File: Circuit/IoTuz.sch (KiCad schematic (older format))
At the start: 29 parts, among them P1 Alligator Connector, P2 BATTERY, P3 USB_5PIN_SHELL, P4 LED_1, P5 LED_2, P6 CONN_01X20, P7 CONN_01X20, Q1 S8050, Q2 S8050, Q3 FDN340P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

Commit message: Updated Alligator tabs
Incomplete.  Included to provide ideas.
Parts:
- P1: footprint libs:aligator_pads -> libs:alligator_pads
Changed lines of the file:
@@
 F 0 "P1" H 6300 7700 50  0000 C CNN
 F 1 "Alligator Connector" V 6400 6950 50  0000 C CNN
-F 2 "libs:aligator_pads" H 6300 6950 50  0001 C CNN
+F 2 "libs:alligator_pads" H 6300 6950 50  0001 C CNN
 F 3 "" H 6300 6950 50  0000 C CNN
 	1    6300 6950

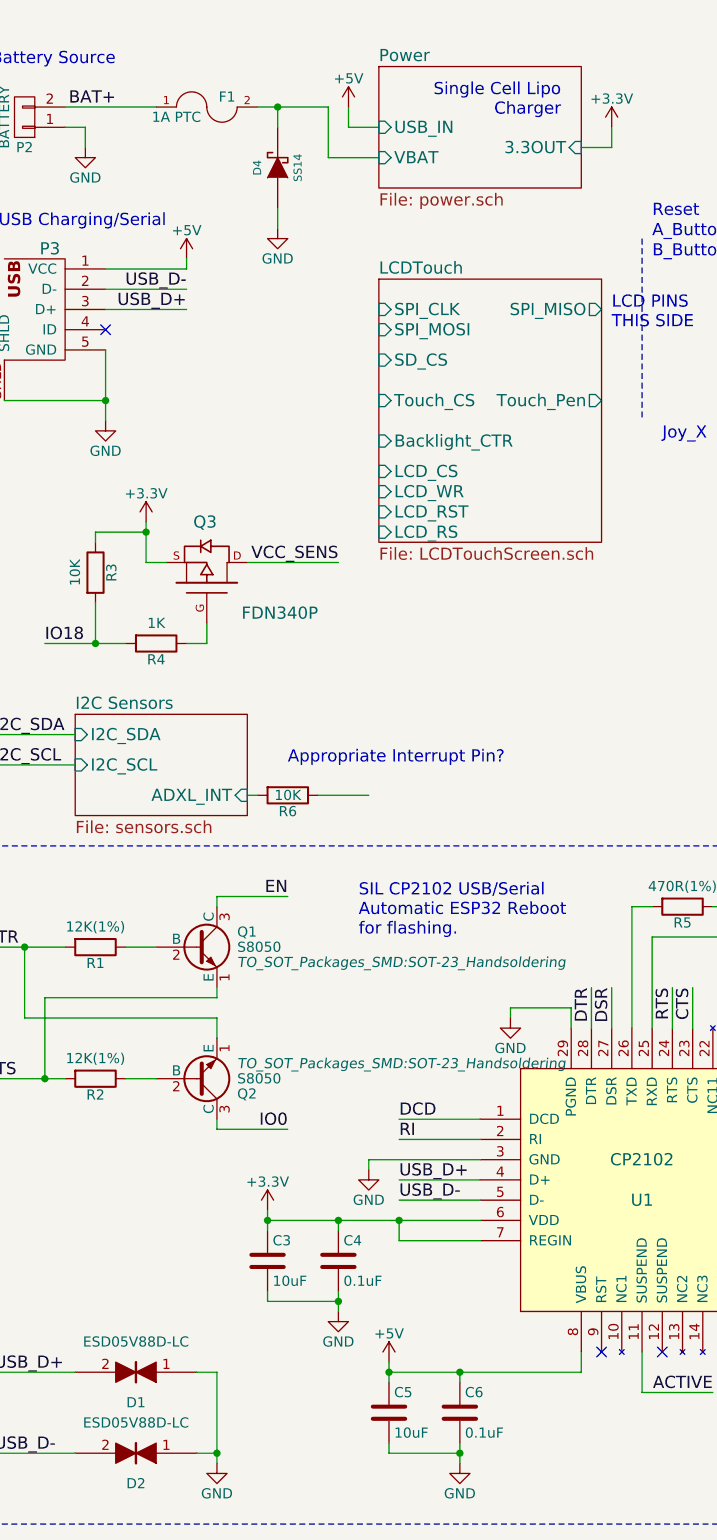
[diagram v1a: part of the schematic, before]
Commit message: BOM information to schematic. Power & main sheets mostly.
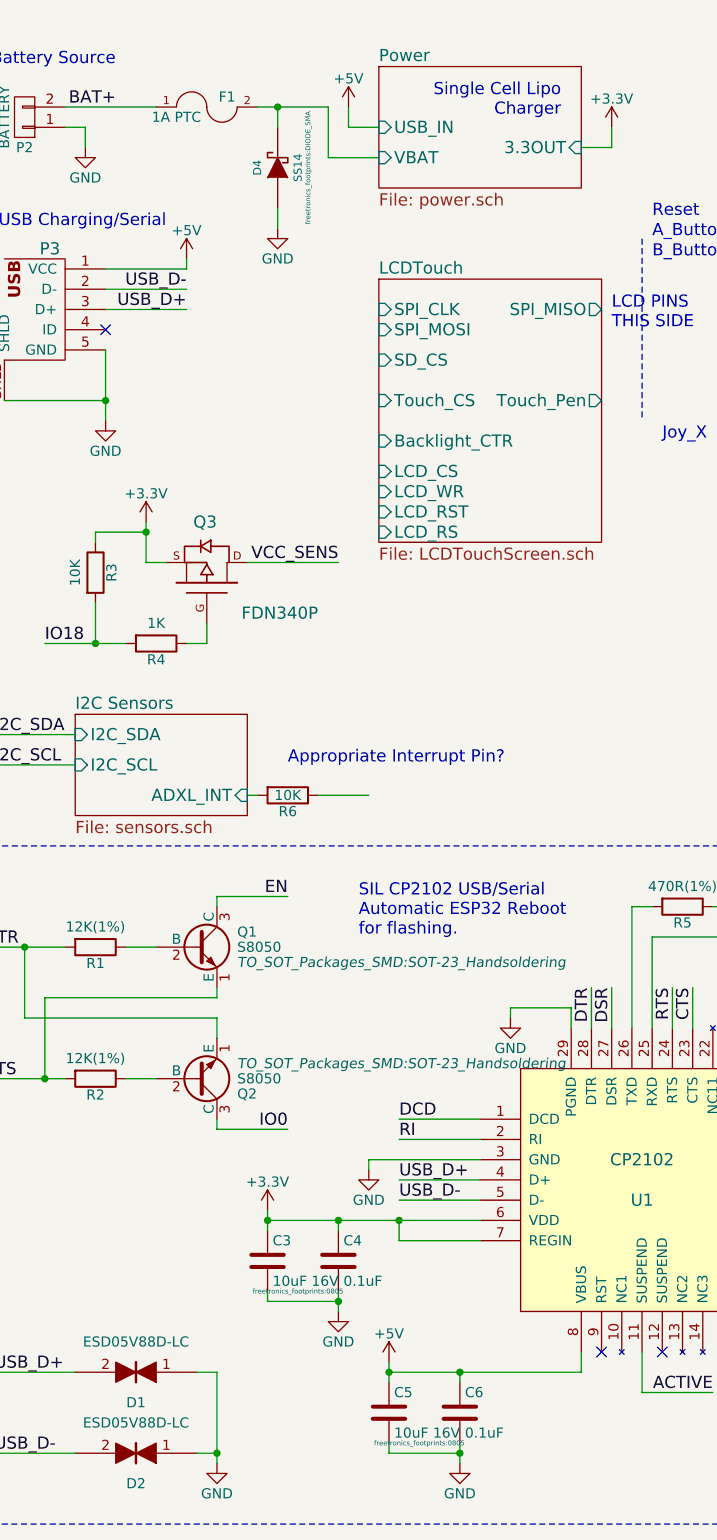
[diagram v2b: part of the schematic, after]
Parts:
- C3, C5: value 10uF -> 10uF 16V; footprint Capacitors_SMD:C_0603_HandSoldering -> freetronics_footprints:0805; Digikey PN (none) -> 1276-2399-1-ND; Link (none) -> http://www.digikey.com.au/product-detail/en/samsung-electro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; Manufacturer PN (none) -> CL21A106KOCLRNC; Unit Cost (none) -> 0.18
- C4, C6: Digikey PN (none) -> 311-1088-1-ND; Link (none) -> http://www.digikey.com.au/product-detail/en/yageo/CC0603KRX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; Manufacturer PN (none) -> CC0603KRX7R7BB104; Unit Cost (none) -> 0.10
- D4: Digikey PN (none) -> SS14CT-ND; Link (none) -> http://www.digikey.com.au/product-detail/en/fairchild-semic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; Manufacturer PN (none) -> SS14; Unit Cost (none) -> 0.39
- P1: footprint libs:alligator_pads -> libs:aligator_pads
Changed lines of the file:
@@
 BAT+
-$Comp
-L DIODE_SCHOTTKY D4
-U 1 1 57FB66B6
-P 2000 1150
-F 0 "D4" H 2000 1250 40  0000 C CNN
-F 1 "SS14" H 2000 1050 40  0000 C CNN
-F 2 "freetronics_footprints:DIODE_SMA" H 2000 1150 60  0001 C CNN
-F 3 "" H 2000 1150 60  0000 C CNN
-	1    2000 1150
-	0    -1   -1   0
-$EndComp
 $Comp
 L GND #PWR03
@@
 $EndComp
 $Comp
-L C C3
-U 1 1 580787A7
-P 1950 6550
-F 0 "C3" H 1975 6650 50  0000 L CNN
-F 1 "10uF" H 1975 6450 50  0000 L CNN
-F 2 "Capacitors_SMD:C_0603_HandSoldering" H 1988 6400 50  0001 C CNN
-F 3 "" H 1950 6550 50  0000 C CNN
-	1    1950 6550
-	1    0    0    -1
-$EndComp
-$Comp
 L C C4
 U 1 1 58078ABF
@@
 F 2 "Capacitors_SMD:C_0603_HandSoldering" H 2338 6400 50  0001 C CNN
 F 3 "" H 2300 6550 50  0000 C CNN
+F 4 "311-1088-1-ND" H 2300 6550 60  0001 C CNN "Digikey PN"
+F 5 "http://www.digikey.com.au/product-detail/en/yageo/CC0603KRX7R7BB104/311-1088-1-ND/302998" H 2300 6550 60  0001 C CNN "Link"
+F 6 "CC0603KRX7R7BB104" H 2300 6550 60  0001 C CNN "Manufacturer PN"
+F 7 "0.10" H 2300 6550 60  0001 C CNN "Unit Cost"
 	1    2300 6550
 	1    0    0    -1
@@
 F 3 "" H 2550 7050 50  0000 C CNN
 	1    2550 7050
-	1    0    0    -1
-$EndComp
-$Comp
-L C C5
-U 1 1 5807AA65
-P 2550 7300
-F 0 "C5" H 2575 7400 50  0000 L CNN
-F 1 "10uF" H 2575 7200 50  0000 L CNN
-F 2 "Capacitors_SMD:C_0603_HandSoldering" H 2588 7150 50  0001 C CNN
-F 3 "" H 2550 7300 50  0000 C CNN
-	1    2550 7300
-	1    0    0    -1
-$EndComp
-$Comp
-L C C6
-U 1 1 5807AADF
-P 2900 7300
-F 0 "C6" H 2925 7400 50  0000 L CNN
-F 1 "0.1uF" H 2925 7200 50  0000 L CNN
-F 2 "Capacitors_SMD:C_0603_HandSoldering" H 2938 7150 50  0001 C CNN
-F 3 "" H 2900 7300 50  0000 C CNN
-	1    2900 7300
 	1    0    0    -1
 $EndComp
@@
 F 0 "P1" H 6300 7700 50  0000 C CNN
 F 1 "Alligator Connector" V 6400 6950 50  0000 C CNN
-F 2 "libs:alligator_pads" H 6300 6950 50  0001 C CNN
+F 2 "libs:aligator_pads" H 6300 6950 50  0001 C CNN
 F 3 "" H 6300 6950 50  0000 C CNN
 	1    6300 6950
@@
 	0    1    1    0
 $EndComp
+$Comp
+L DIODE_SCHOTTKY D4
+U 1 1 5821353B
+P 2000 1150
+F 0 "D4" H 2000 1250 40  0000 C CNN
+F 1 "SS14" H 2000 1050 40  0000 C CNN
+F 2 "freetronics_footprints:DIODE_SMA" H 2000 1000 24  0000 C CNN
+F 3 "" H 2000 1150 60  0000 C CNN
+F 4 "SS14CT-ND" H 2000 1150 60  0001 C CNN "Digikey PN"
+F 5 "http://www.digikey.com.au/product-detail/en/fairchild-semiconductor/SS14/SS14CT-ND/965729" H 2000 1150 60  0001 C CNN "Link"
+F 6 "SS14" H 2000 1150 60  0001 C CNN "Manufacturer PN"
+F 7 "0.39" H 2000 1150 60  0001 C CNN "Unit Cost"
+	1    2000 1150
+	0    -1   -1   0
+$EndComp
+$Comp
+L C C3
+U 1 1 582193F3
+P 1950 6550
+F 0 "C3" H 1975 6650 50  0000 L CNN
+F 1 "10uF 16V" H 1975 6450 50  0000 L CNN
+F 2 "freetronics_footprints:0805" H 2100 6400 24  0000 C CNN
+F 3 "" H 1950 6550 60  0000 C CNN
+F 4 "1276-2399-1-ND" H 1950 6550 60  0001 C CNN "Digikey PN"
+F 5 "http://www.digikey.com.au/product-detail/en/samsung-electro-mechanics-america-inc/CL21A106KOCLRNC/1276-2399-1-ND/3890485" H 1950 6550 60  0001 C CNN "Link"
+F 6 "CL21A106KOCLRNC" H 1950 6550 60  0001 C CNN "Manufacturer PN"
+F 7 "0.18" H 1950 6550 60  0001 C CNN "Unit Cost"
+	1    1950 6550
+	1    0    0    -1
+$EndComp
+$Comp
+L C C5
+U 1 1 58219789
+P 2550 7300
+F 0 "C5" H 2575 7400 50  0000 L CNN
+F 1 "10uF 16V" H 2575 7200 50  0000 L CNN
+F 2 "freetronics_footprints:0805" H 2700 7150 24  0000 C CNN
+F 3 "" H 2550 7300 60  0000 C CNN
+F 4 "1276-2399-1-ND" H 2550 7300 60  0001 C CNN "Digikey PN"
+F 5 "http://www.digikey.com.au/product-detail/en/samsung-electro-mechanics-america-inc/CL21A106KOCLRNC/1276-2399-1-ND/3890485" H 2550 7300 60  0001 C CNN "Link"
+F 6 "CL21A106KOCLRNC" H 2550 7300 60  0001 C CNN "Manufacturer PN"
+F 7 "0.18" H 2550 7300 60  0001 C CNN "Unit Cost"
+	1    2550 7300
+	1    0    0    -1
+$EndComp
+$Comp
+L C C6
+U 1 1 5821E550
+P 2900 7300
+F 0 "C6" H 2925 7400 50  0000 L CNN
+F 1 "0.1uF" H 2925 7200 50  0000 L CNN
+F 2 "Capacitors_SMD:C_0603_HandSoldering" H 2938 7150 50  0001 C CNN
+F 3 "" H 2900 7300 50  0000 C CNN
+F 4 "311-1088-1-ND" H 2900 7300 60  0001 C CNN "Digikey PN"
+F 5 "http://www.digikey.com.au/product-detail/en/yageo/CC0603KRX7R7BB104/311-1088-1-ND/302998" H 2900 7300 60  0001 C CNN "Link"
+F 6 "CC0603KRX7R7BB104" H 2900 7300 60  0001 C CNN "Manufacturer PN"
+F 7 "0.10" H 2900 7300 60  0001 C CNN "Unit Cost"
+	1    2900 7300
+	1    0    0    -1
+$EndComp
 $EndSCHEMATC

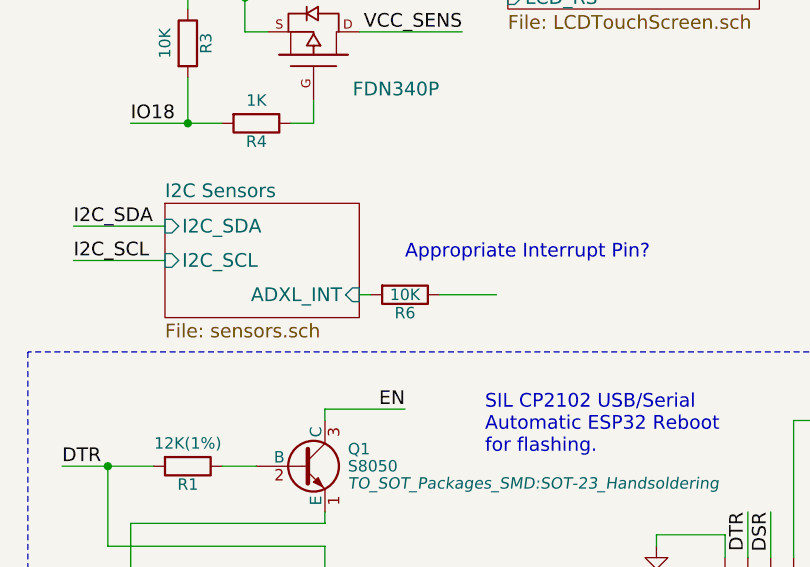
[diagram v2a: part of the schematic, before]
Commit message: More BOM - passives mostly.
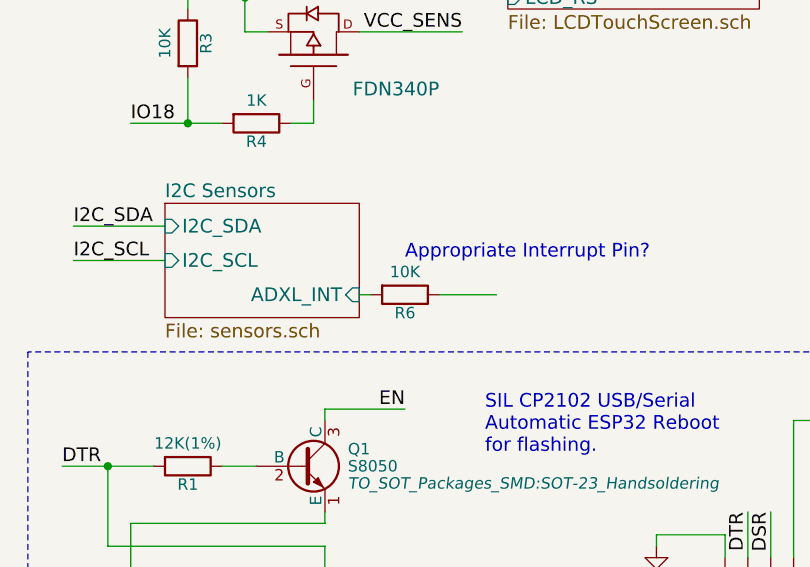
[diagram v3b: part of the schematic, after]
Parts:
- F1: Digikey PN (none) -> 507-1786-1-ND; Link (none) -> http://www.digikey.com.au/product-detail/en/bel-fuse-inc/0Z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; Manufacturer PN (none) -> 0ZCH0050FF2G; Unit Cost (none) -> 0.12
- R3, R6: Digikey PN (none) -> 311-10KGRCT-ND; Link (none) -> http://www.digikey.com.au/product-detail/en/yageo/RC0603JR-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; Manufacturer PN (none) -> RC0603JR-0710KL; Unit Cost (none) -> 0.10
- R4: Digikey PN (none) -> 311-1.0KGRCT-ND; Link (none) -> http://www.digikey.com.au/product-detail/en/yageo/RC0603JR-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; Manufacturer PN (none) -> RC0603JR-071KL; Unit Cost (none) -> 0.10
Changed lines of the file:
@@
 F 2 "freetronics_footprints:1210" H 1650 850 50  0001 C CNN
 F 3 "" H 1650 850 50  0000 C CNN
+F 4 "507-1786-1-ND" H 1650 850 60  0001 C CNN "Digikey PN"
+F 5 "http://www.digikey.com.au/product-detail/en/bel-fuse-inc/0ZCH0050FF2G/507-1786-1-ND/4156209" H 1650 850 60  0001 C CNN "Link"
+F 6 "0ZCH0050FF2G" H 1650 850 60  0001 C CNN "Manufacturer PN"
+F 7 "0.12" H 1650 850 60  0001 C CNN "Unit Cost"
 	1    1650 850
 	1    0    0    -1
@@
 F 2 "Resistors_SMD:R_0603_HandSoldering" V 1030 3150 50  0001 C CNN
 F 3 "" H 1100 3150 50  0000 C CNN
+F 4 "311-10KGRCT-ND" V 1100 3150 60  0001 C CNN "Digikey PN"
+F 5 "http://www.digikey.com.au/product-detail/en/yageo/RC0603JR-0710KL/311-10KGRCT-ND/729647" V 1100 3150 60  0001 C CNN "Link"
+F 6 "RC0603JR-0710KL" V 1100 3150 60  0001 C CNN "Manufacturer PN"
+F 7 "0.10" V 1100 3150 60  0001 C CNN "Unit Cost"
 	1    1100 3150
 	1    0    0    -1
@@
 F 2 "Resistors_SMD:R_0603_HandSoldering" V 1330 3500 50  0001 C CNN
 F 3 "" H 1400 3500 50  0000 C CNN
+F 4 "311-1.0KGRCT-ND" V 1400 3500 60  0001 C CNN "Digikey PN"
+F 5 "http://www.digikey.com.au/product-detail/en/yageo/RC0603JR-071KL/311-1.0KGRCT-ND/729624" V 1400 3500 60  0001 C CNN "Link"
+F 6 "RC0603JR-071KL" V 1400 3500 60  0001 C CNN "Manufacturer PN"
+F 7 "0.10" V 1400 3500 60  0001 C CNN "Unit Cost"
 	1    1400 3500
 	0    1    1    0
@@
 Text Label 600  4100 0    60   ~ 0
 I2C_SCL
-$Comp
-L R R6
-U 1 1 5812B9CE
-P 2050 4250
-F 0 "R6" V 2130 4250 50  0000 C CNN
-F 1 "10K" V 2050 4250 50  0000 C CNN
-F 2 "Resistors_SMD:R_0603_HandSoldering" V 1980 4250 50  0001 C CNN
-F 3 "" H 2050 4250 50  0000 C CNN
-	1    2050 4250
-	0    1    1    0
-$EndComp
 $Sheet
 S 9200 5550 1500 800
@@
 	1    0    0    -1
 $EndComp
+$Comp
+L R R6
+U 1 1 582211E2
+P 2050 4250
+F 0 "R6" V 2130 4250 50  0000 C CNN
+F 1 "10K" V 1950 4250 50  0000 C CNN
+F 2 "Resistors_SMD:R_0603_HandSoldering" V 1980 4250 50  0001 C CNN
+F 3 "" H 2050 4250 50  0000 C CNN
+F 4 "311-10KGRCT-ND" V 2050 4250 60  0001 C CNN "Digikey PN"
+F 5 "http://www.digikey.com.au/product-detail/en/yageo/RC0603JR-0710KL/311-10KGRCT-ND/729647" V 2050 4250 60  0001 C CNN "Link"
+F 6 "RC0603JR-0710KL" V 2050 4250 60  0001 C CNN "Manufacturer PN"
+F 7 "0.10" V 2050 4250 60  0001 C CNN "Unit Cost"
+	1    2050 4250
+	0    1    1    0
+$EndComp
 $EndSCHEMATC

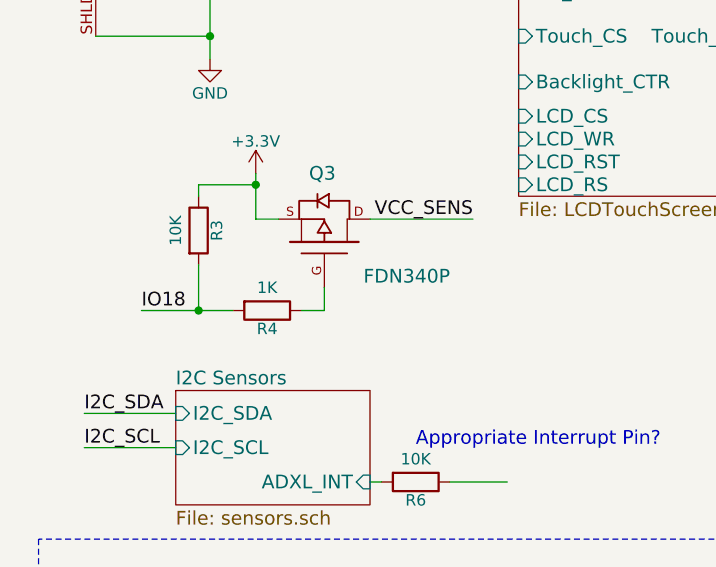
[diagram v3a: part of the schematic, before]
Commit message: BOM. Some passives & transistors. Nearly done.
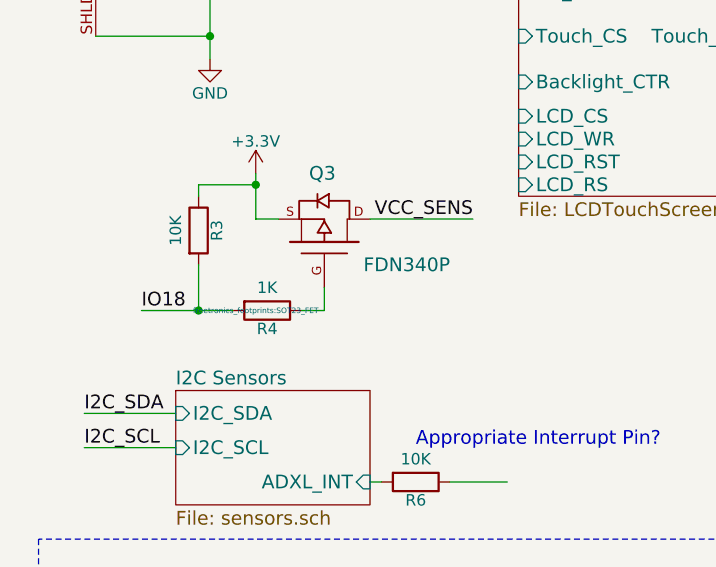
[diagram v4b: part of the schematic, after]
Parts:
- C11: Digikey PN (none) -> 490-3184-1-ND; Link (none) -> http://www.digikey.com.au/product-detail/en/murata-electron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; Manufacturer PN (none) -> GRM033R71E102KA01D; Unit Cost (none) -> 0.10
- Q3: Digikey PN (none) -> FDN340PCT-ND; Link (none) -> http://www.digikey.com.au/product-detail/en/fairchild-semic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; Manufacturer PN (none) -> FDN340P; Unit Cost (none) -> 0.39
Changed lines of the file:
@@
 	0    1    1    0
-$EndComp
-$Comp
-L C C11
-U 1 1 58086D6E
-P 10550 1200
-F 0 "C11" H 10575 1300 50  0000 L CNN
-F 1 "1nF" H 10575 1100 50  0000 L CNN
-F 2 "Capacitors_SMD:C_0603_HandSoldering" H 10588 1050 50  0001 C CNN
-F 3 "" H 10550 1200 50  0000 C CNN
-	1    10550 1200
-	1    0    0    -1
 $EndComp
 Text Label 11150 800  2    60   ~ 0
@@
 	1    8700 1100
 	1    0    0    -1
-$EndComp
-$Comp
-L MOSFET_P Q3
-U 1 1 580E31AD
-P 1650 3200
-F 0 "Q3" V 1950 3250 60  0000 R CNN
-F 1 "FDN340P" V 1500 3750 60  0000 R CNN
-F 2 "freetronics_footprints:SOT23_FET" H 1650 3200 60  0001 C CNN
-F 3 "" H 1650 3200 60  0000 C CNN
-	1    1650 3200
-	0    1    -1   0
 $EndComp
 Text Label 2300 3100 2    60   ~ 0
@@
 	0    1    1    0
 $EndComp
+$Comp
+L MOSFET_P Q3
+U 1 1 5822CF95
+P 1650 3200
+F 0 "Q3" V 1950 3250 60  0000 R CNN
+F 1 "FDN340P" V 1550 3750 60  0000 R CNN
+F 2 "freetronics_footprints:SOT23_FET" V 1350 2900 24  0000 C CNN
+F 3 "" H 1650 3200 60  0000 C CNN
+F 4 "FDN340PCT-ND" V 1650 3200 60  0001 C CNN "Digikey PN"
+F 5 "http://www.digikey.com.au/product-detail/en/fairchild-semiconductor/FDN340P/FDN340PCT-ND/965604" V 1650 3200 60  0001 C CNN "Link"
+F 6 "FDN340P" V 1650 3200 60  0001 C CNN "Manufacturer PN"
+F 7 "0.39" V 1650 3200 60  0001 C CNN "Unit Cost"
+	1    1650 3200
+	0    1    -1   0
+$EndComp
+$Comp
+L C C11
+U 1 1 58230BE0
+P 10550 1200
+F 0 "C11" H 10575 1300 50  0000 L CNN
+F 1 "1nF" H 10575 1100 50  0000 L CNN
+F 2 "Capacitors_SMD:C_0603_HandSoldering" H 10588 1050 50  0001 C CNN
+F 3 "" H 10550 1200 50  0000 C CNN
+F 4 "490-3184-1-ND" H 10550 1200 60  0001 C CNN "Digikey PN"
+F 5 "http://www.digikey.com.au/product-detail/en/murata-electronics-north-america/GRM033R71E102KA01D/490-3184-1-ND/702725" H 10550 1200 60  0001 C CNN "Link"
+F 6 "GRM033R71E102KA01D" H 10550 1200 60  0001 C CNN "Manufacturer PN"
+F 7 "0.10" H 10550 1200 60  0001 C CNN "Unit Cost"
+	1    10550 1200
+	1    0    0    -1
+$EndComp
 $EndSCHEMATC

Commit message: Sensor ICs BOM information.
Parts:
- P4, P5, U2: Non-Digikey (none) -> 1
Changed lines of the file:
@@
 F 2 "ESP32-footprints-Lib:ESP32-WROOM" H 6100 3250 60  0001 C CNN
 F 3 "" H 5300 2350 60  0001 C CNN
+F 4 "1" H 5750 1900 60  0001 C CNN "Non-Digikey"
 	1    5750 1900
 	1    0    0    -1
@@
 F 2 "libs:LED_8MM_APA-106" H 8050 650 50  0001 C CNN
 F 3 "" H 8050 650 50  0000 C CNN
+F 4 "1" H 8050 650 60  0001 C CNN "Non-Digikey"
 	1    8050 650
 	0    -1   -1   0
@@
 F 2 "libs:LED_8MM_APA-106" H 8550 650 50  0001 C CNN
 F 3 "" H 8550 650 50  0000 C CNN
+F 4 "1" H 8550 650 60  0001 C CNN "Non-Digikey"
 	1    8550 650
 	0    -1   -1   0

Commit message: Schematic notes.
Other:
- note added: "Need to add serial programming header?"
- note added: "REMOVE?"
- moved on the sheet: P6, P7
